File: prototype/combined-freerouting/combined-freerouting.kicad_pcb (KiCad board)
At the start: 2 copper layers, 70.3 x 215.8 mm, 179 parts, among them J1 FFC2B21-40-T_REVA, J2 battery, J3 5530843-5, J4 USB4105-GF-A, J5 5530843-5, J7 640456-3, J8 Micro_SD_Card, SW10 KP_MODLOCK, SW11 KP_LEFT, SW12 KP_OK, SW13 KP_RIGHT, SW14 KP_HELP, SW15 KP_PROG, SW16 KP_MENU, SW17 KP_BACK, SW18 KP_DOWN, SW19 KP_TASKS, SW2 MODE_SWITCH, SW20 KP_FUNCS, SW4 KP_CTRL, SW5 KP_SHIFT, SW6 KP_UP, SW7 KP_HOME, SW8 KP_POWER, SW9 KP_ALT, U1 RP2040, U11 TPS22919DCKR, U12 CD4053B, U13 FSUSB42MUX, U14 KTS1622EUAA-TR, U17 RESET_BTN, U18 SN74HCT373PWR, U2 BQ21040DBVR, U3 TPS613221ADBVR, U5 ESP32-C6-MINI-1-H4, U6 W25Q32JVSSIQ, U7 KTS1622EUAA-TR, U8 TPS22919DCKR, U9 FLASH_BTN, Y1 12MHz

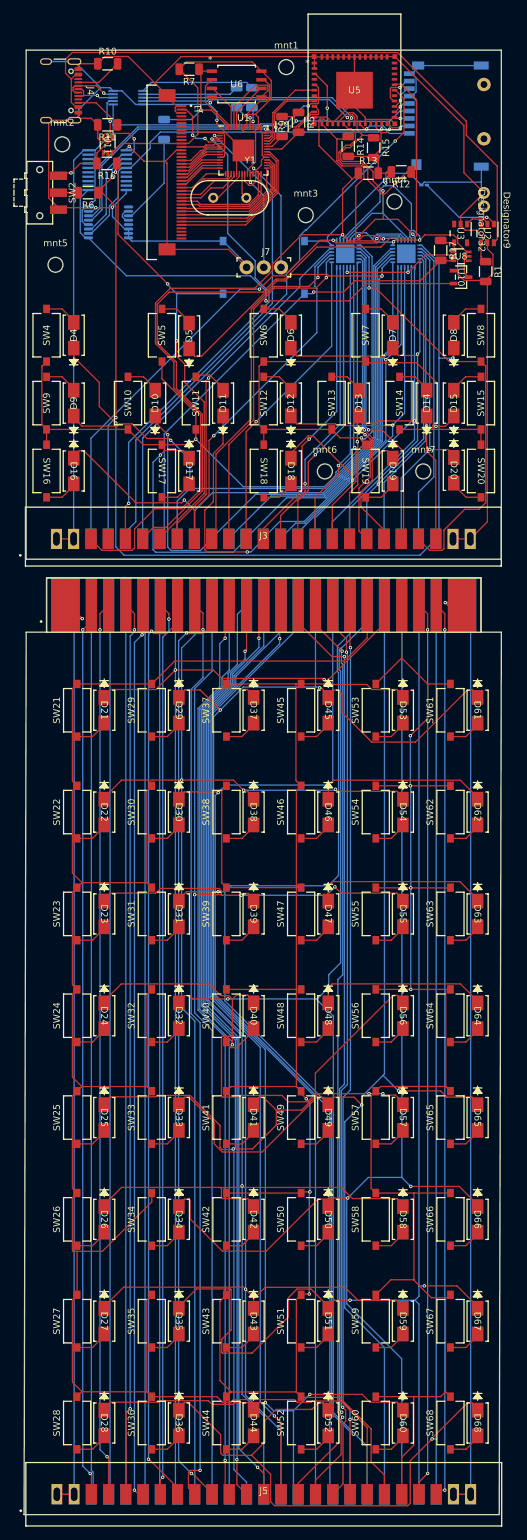
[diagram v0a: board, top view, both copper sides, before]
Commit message: finished calculator & mathboard PCBs, updated pricing calc
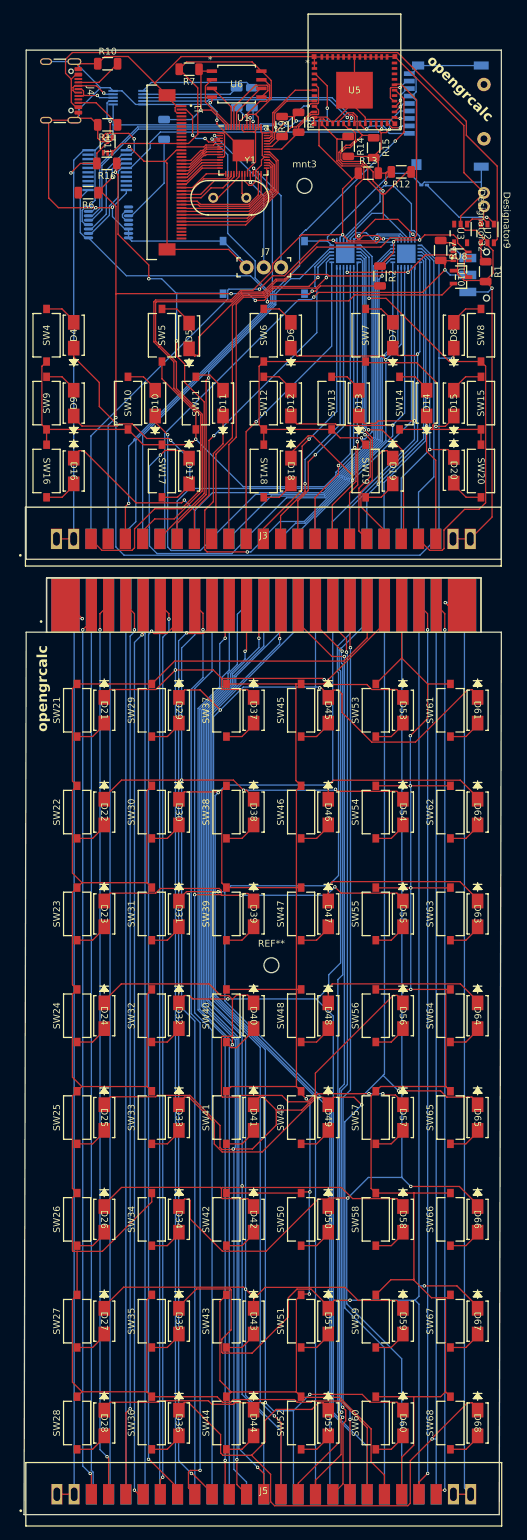
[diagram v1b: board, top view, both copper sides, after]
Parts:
- removed mnt1, mnt2, mnt4, mnt5, mnt6, mnt7: MountingHole_2.2mm_M2, MountingHole:MountingHole_2.2mm_M2
- added R2: 10k, Resistor_SMD:R_1206_3216Metric, F.Cu at (72.1, 53.3)
- added REF**: MountingHole_2.2mm_M2, MountingHole:MountingHole_2.2mm_M2, F.Cu at (56.1, 154.8)
- SW2: value MODE_SWITCH -> PWR_SWITCH; moved to B.Cu
- U17: value RESET_BTN -> MODE_BTN
- moved SW2 66.9 mm to (87.8, 53.1)
- moved mnt3 4.32 mm to (61.0, 40.0)
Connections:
- SW2 pad 1: +3.3V -> VCC
- SW2 pad 2: Net-(SW2-B) -> /GLOBAL_RESET_PIN
- U17 pad 2: /GLOBAL_RESET_PIN -> /MODE_PIN
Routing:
- net /MODE_PIN: track 59.7 -> 100.6 mm, vias 2 -> 5
- net GND: track 546.4 -> 538.8 mm, vias 8 -> 9
- net /GLOBAL_RESET_PIN: track 68.9 -> 74.3 mm, vias 1 -> 2
- net /mathboard/b8: track 187.4 -> 182.5 mm
- net /mathboard/b9: track 189.6 -> 185.2 mm
- net /mathboard/esp_rx: track 131.2 -> 126.9 mm
- net /mathboard/a3: track 247.1 -> 243.5 mm
- net /mathboard/a15: track 136.4 -> 132.8 mm
- net /mathboard/b4: track 184.3 -> 181.2 mm
- net /mathboard/a13: track 136.8 -> 133.7 mm
- net /mathboard/3v3: track 138.6 -> 135.6 mm
- net /mathboard/a6: track 133.3 -> 130.3 mm
- net Net-(SW2-B): track 2.91 -> 0.00 mm
- net /mathboard/a7: track 135.0 -> 132.1 mm
- net /mathboard/a8: track 138.0 -> 135.4 mm
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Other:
- board text added: "opengrcalc"

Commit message: added support for constant prices, taxes, and fixed bulk quantities to the pricing calculator; fixed error in the PCB's edge cuts
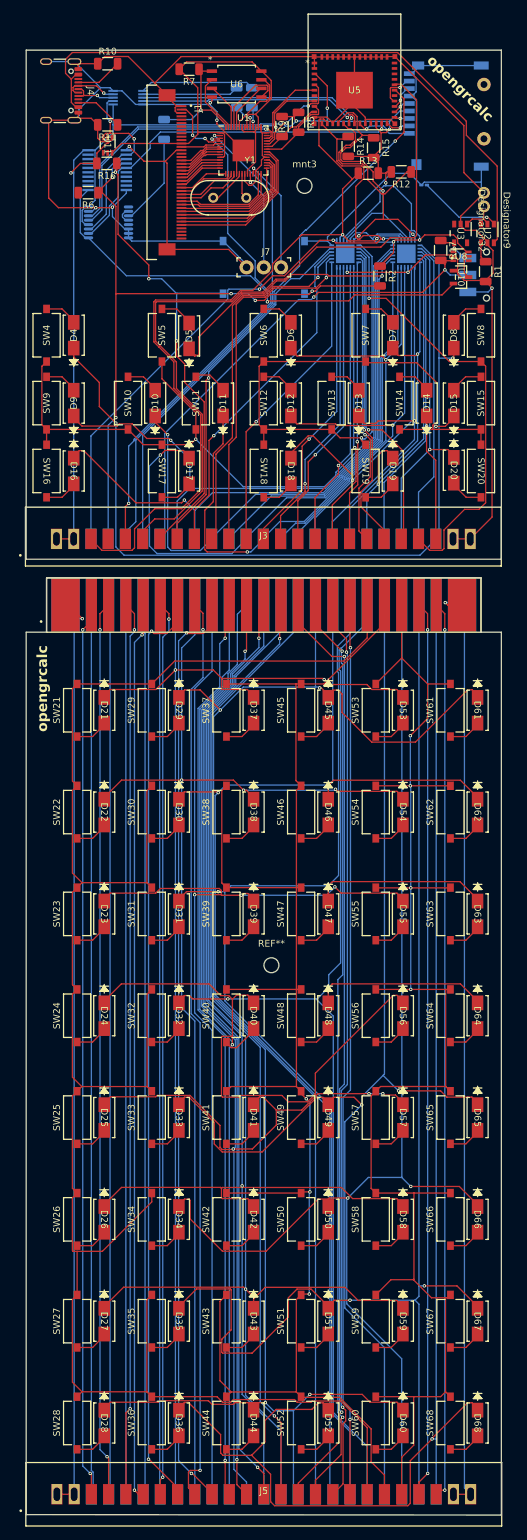
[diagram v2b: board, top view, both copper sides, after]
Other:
- board size 70.3 x 215.8 mm -> 70 x 215.8 mm
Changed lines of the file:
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@@
     (fp_line (start 1.6 0.8) (end -1.6 0.8)
       (stroke (width 0.1) (type solid)) (layer "F.Fab"))
-    (pad "1" smd roundrect (at -1.4625 0 270) (size 1.125 1.75) (layers "F.Cu" "F.Paste" "F.Mask") (roundrect_rratio 0.222222)
+    (pad "1" smd roundrect (at -1.4625 0 270) (size 1.125 1.75) (layers "F.Cu" "F.Paste" "F.Mask") (roundrect_rratio 0.2222222222)
       (net 48 "+3.3V") (pintype "passive"))
-    (pad "2" smd roundrect (at 1.4625 0 270) (size 1.125 1.75) (layers "F.Cu" "F.Paste" "F.Mask") (roundrect_rratio 0.222222)
+    (pad "2" smd roundrect (at 1.4625 0 270) (size 1.125 1.75) (layers "F.Cu" "F.Paste" "F.Mask") (roundrect_rratio 0.2222222222)
       (net 130 "/MODE_PIN") (pintype "passive"))
     (model "${KICAD6_3DMODEL_DIR}/Resistor_SMD.3dshapes/R_1206_3216Metric.wrl"
@@
       (xy 87 105.75)
       (xy 90 105.75)
-      (xy 89.6875 235.75)
-      (xy 19.6875 235.75)
+      (xy 90 235.8125)
+      (xy 20 235.75)
     )
     (stroke (width 0.1) (type solid)) (fill none) (layer "Edge.Cuts"))
